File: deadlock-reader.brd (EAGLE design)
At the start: 49.2 x 49.5 mm, 49 parts, among them IC1 LM386M-1, IC2 STM32F072XX, IC3 MCP16301/H, IC4 MAX3232CSE, J1 RJ12 6p6c, X1 MINI-USB-SCHIELD-32005-301

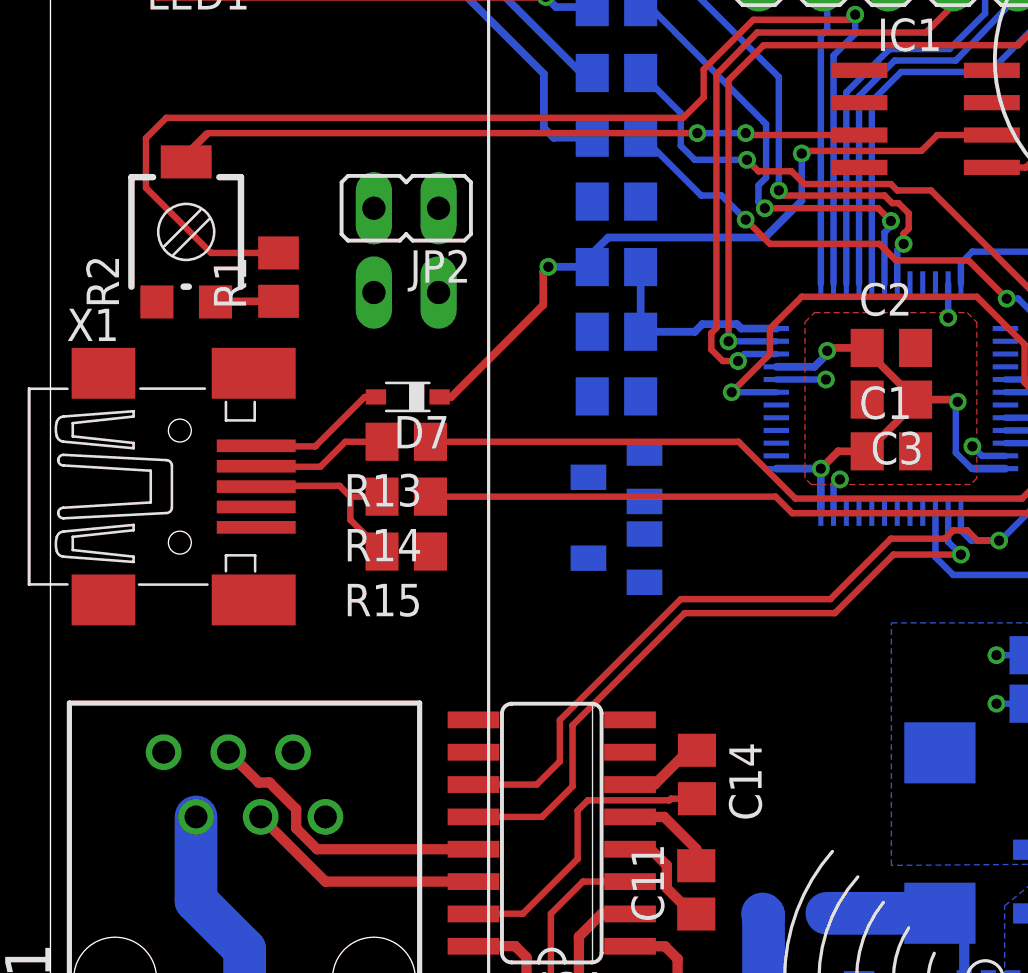
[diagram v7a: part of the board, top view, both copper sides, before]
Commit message: [WIP] Route misc remaining signal lines
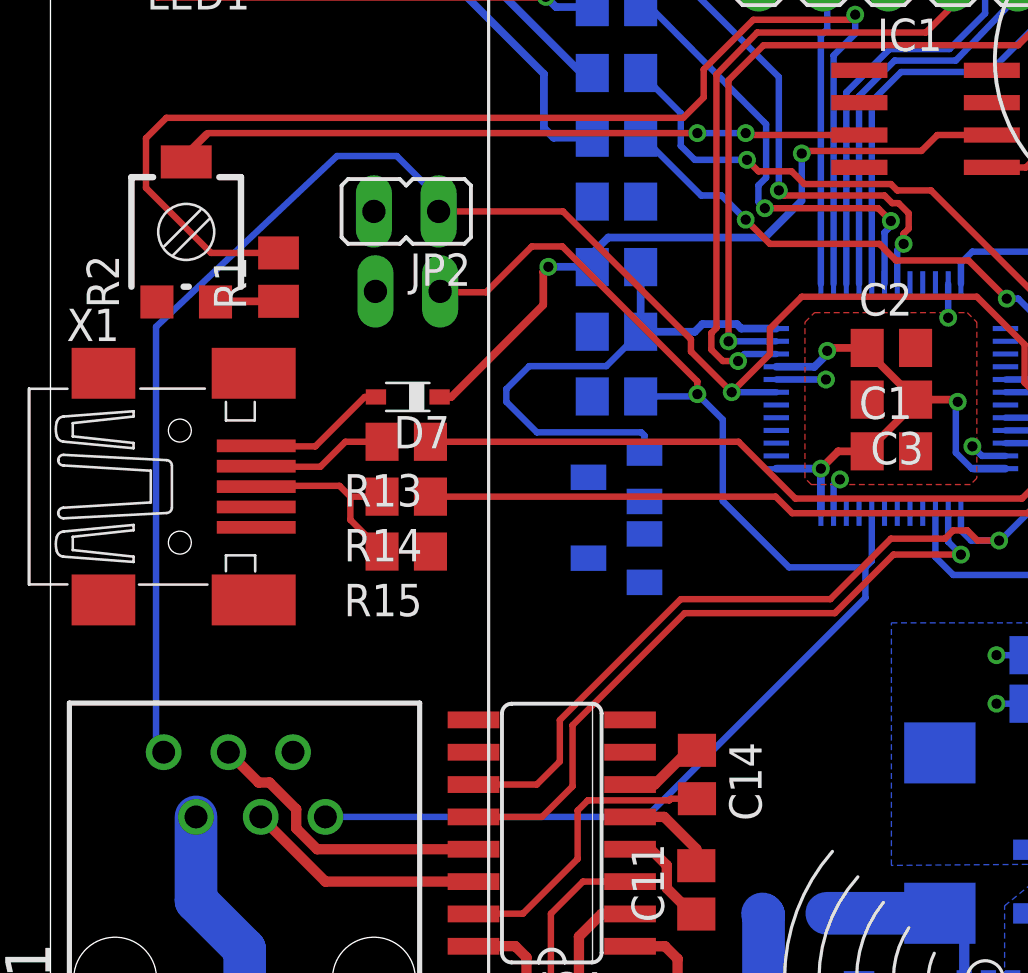
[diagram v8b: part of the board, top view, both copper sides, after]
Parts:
- moved JP2 0.12 mm to (14.0, 36.5)
- moved JP1 0.07 mm to (14.0, 33.3), turned to 270 degrees
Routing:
- net BOOT0: track 0.00 -> 55.3 mm, vias 0 -> 1
- net RST: track 29.1 -> 75.7 mm
- net V_SENSE: track 8.06 -> 21.4 mm
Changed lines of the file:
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@@
 <setting verticaltext="up"/>
 </settings>
-<grid distance="0.05" unitdist="mm" unit="mm" style="dots" multiple="5" display="yes" altdistance="0.125" altunitdist="mm" altunit="mm"/>
+<grid distance="0.1" unitdist="mm" unit="mm" style="dots" multiple="5" display="yes" altdistance="0.125" altunitdist="mm" altunit="mm"/>
 <layers>
 <layer number="1" name="Top" color="4" fill="1" visible="yes" active="yes"/>
@@
 <attribute name="MF" value="" x="7.62" y="6.35" size="1.778" layer="27" display="off"/>
 </element>
-<element name="JP1" library="jumper" package="JP1" value="BOOT" x="13.97" y="33.29" rot="MR90"/>
-<element name="JP2" library="jumper" package="JP1" value="RESET" x="13.97" y="36.6" rot="R90"/>
+<element name="JP1" library="jumper" package="JP1" value="BOOT" x="14.03" y="33.335" rot="MR270"/>
+<element name="JP2" library="jumper" package="JP1" value="RESET" x="13.97" y="36.475" rot="R90"/>
 <element name="JP3" library="pinhead" package="1X06" value="" x="45.74" y="28.545" rot="MR270"/>
 <element name="L1" library="rcl" package="PIS2816" value="15uH" x="42.545" y="12.065" rot="MR180"/>
@@
 <wire x1="2.08" y1="30.12" x2="4.18" y2="32.92" width="0" layer="19" extent="1-1"/>
 <wire x1="2.08" y1="21.22" x2="7.98" y2="21.22" width="0" layer="19" extent="1-1"/>
-<wire x1="12.7" y1="36.6" x2="7.98" y2="30.12" width="0" layer="19" extent="1-1"/>
-<wire x1="9.93" y1="46.75" x2="12.7" y2="36.6" width="0" layer="19" extent="1-1"/>
+<wire x1="12.7" y1="36.475" x2="7.98" y2="30.12" width="0" layer="19" extent="1-1"/>
+<wire x1="9.93" y1="46.75" x2="12.7" y2="36.475" width="0" layer="19" extent="1-1"/>
 </signal>
 <signal name="N$1">
@@
 <contactref element="JP1" pad="1"/>
 <contactref element="R6" pad="2"/>
-<wire x1="23.175" y1="29.21" x2="32.25" y2="24.625" width="0" layer="19" extent="16-16"/>
-<wire x1="12.7" y1="33.29" x2="23.175" y2="29.21" width="0" layer="19" extent="16-16"/>
-<wire x1="10.795" y1="12.7" x2="23.175" y2="29.21" width="0" layer="19" extent="16-16"/>
+<wire x1="32.25" y1="24.625" x2="32.25" y2="22.75" width="0.254" layer="16"/>
+<wire x1="32.25" y1="22.75" x2="32" y2="22.5" width="0.254" layer="16"/>
+<wire x1="32" y1="22.5" x2="29" y2="22.5" width="0.254" layer="16"/>
+<wire x1="29" y1="22.5" x2="26.4" y2="25.1" width="0.254" layer="16"/>
+<wire x1="26.4" y1="25.1" x2="26.4" y2="28.3" width="0.254" layer="16"/>
+<wire x1="26.4" y1="28.3" x2="25.4" y2="29.3" width="0.254" layer="16"/>
+<via x="25.4" y="29.3" extent="1-16" drill="0.4"/>
+<wire x1="25.4" y1="29.3" x2="25.4" y2="29.8" width="0.254" layer="1"/>
+<wire x1="25.4" y1="29.8" x2="20.1" y2="35.1" width="0.254" layer="1"/>
+<wire x1="20.1" y1="35.1" x2="18.9" y2="35.1" width="0.254" layer="1"/>
+<wire x1="18.9" y1="35.1" x2="17.1" y2="33.3" width="0.254" layer="1"/>
+<wire x1="17.1" y1="33.3" x2="15.335" y2="33.3" width="0.254" layer="1"/>
+<wire x1="15.335" y1="33.3" x2="15.3" y2="33.335" width="0.254" layer="1"/>
+<wire x1="10.795" y1="12.7" x2="23.4" y2="12.7" width="0.254" layer="16"/>
+<wire x1="23.4" y1="12.7" x2="32" y2="21.3" width="0.254" layer="16"/>
+<wire x1="32" y1="21.3" x2="32" y2="22.5" width="0.254" layer="16"/>
+<wire x1="23.175" y1="29.21" x2="25.31" y2="29.21" width="0.254" layer="16"/>
+<wire x1="25.31" y1="29.21" x2="25.4" y2="29.3" width="0.254" layer="16"/>
 </signal>
 <signal name="RST">
@@
 <via x="26.75" y="29.375" extent="1-16" drill="0.4"/>
 <wire x1="26.75" y1="29.375" x2="28.5" y2="29.375" width="0.254" layer="16"/>
-<wire x1="15.24" y1="36.6" x2="26.75" y2="29.375" width="0" layer="19" extent="1-1"/>
-<wire x1="4.445" y1="15.24" x2="15.24" y2="36.6" width="0" layer="19" extent="1-1"/>
+<wire x1="15.24" y1="36.475" x2="20.125" y2="36.475" width="0.254" layer="1"/>
+<wire x1="20.125" y1="36.475" x2="25.15" y2="31.45" width="0.254" layer="1"/>
+<wire x1="25.15" y1="31.45" x2="25.15" y2="30.975" width="0.254" layer="1"/>
+<wire x1="25.15" y1="30.975" x2="26.75" y2="29.375" width="0.254" layer="1"/>
+<wire x1="4.145" y1="31.945" x2="11.25" y2="38.65" width="0.254" layer="16"/>
+<wire x1="11.25" y1="38.65" x2="13.6" y2="38.65" width="0.254" layer="16"/>
+<wire x1="13.6" y1="38.65" x2="15.1" y2="37.15" width="0.254" layer="16"/>
+<wire x1="15.1" y1="37.15" x2="15.1" y2="36.615" width="0.254" layer="16"/>
+<wire x1="15.1" y1="36.615" x2="15.24" y2="36.475" width="0.254" layer="16"/>
+<wire x1="4.145" y1="31.945" x2="4.145" y2="15.54" width="0.254" layer="16"/>
+<wire x1="4.145" y1="15.54" x2="4.445" y2="15.24" width="0.254" layer="16"/>
 </signal>
 <signal name="RDR_TXD/SWDIO">
@@
 <wire x1="16.6166" y1="7.625" x2="16.6116" y2="7.62" width="0.4064" layer="1"/>
 <wire x1="21.275" y1="36.86" x2="27.815" y2="45.845" width="0" layer="19" extent="16-16"/>
-<wire x1="15.24" y1="33.29" x2="21.275" y2="36.86" width="0" layer="19" extent="16-16"/>
-<wire x1="21.125" y1="26.035" x2="15.24" y2="33.29" width="0" layer="19" extent="16-16"/>
-<wire x1="23.325" y1="23.81" x2="21.125" y2="26.035" width="0" layer="19" extent="16-16"/>
-<wire x1="28.5" y1="26.375" x2="23.325" y2="23.81" width="0" layer="19" extent="16-16"/>
+<wire x1="12.76" y1="33.335" x2="21.275" y2="36.86" width="0" layer="19" extent="16-16"/>
+<wire x1="28.5" y1="30.375" x2="21.275" y2="36.86" width="0" layer="19" extent="16-16"/>
 <wire x1="35.75" y1="33.625" x2="32.07" y2="31.115" width="0" layer="19" extent="1-16"/>
+<wire x1="23.325" y1="23.81" x2="28.5" y2="26.375" width="0" layer="19" extent="16-16"/>
+<wire x1="21.125" y1="26.035" x2="23.325" y2="23.81" width="0" layer="19" extent="16-16"/>
 <wire x1="14.92" y1="23.12" x2="21.125" y2="26.035" width="0" layer="19" extent="1-16"/>
 <wire x1="41.38" y1="19.05" x2="37.5" y2="26.375" width="0" layer="19" extent="16-16"/>
@@
 <wire x1="25.3" y1="31.75" x2="23.175" y2="31.75" width="0.3048" layer="16"/>
 <wire x1="26.95" y1="32.05" x2="25.6" y2="32.05" width="0.3048" layer="16"/>
-<wire x1="23.325" y1="26.985" x2="23.175" y2="31.75" width="0" layer="19" extent="16-16"/>
+<wire x1="23.325" y1="26.985" x2="23.325" y2="27.675" width="0.254" layer="16"/>
+<wire x1="23.325" y1="27.675" x2="23.2" y2="27.8" width="0.254" layer="16"/>
+<wire x1="23.2" y1="27.8" x2="19.1" y2="27.8" width="0.254" layer="16"/>
+<wire x1="19.1" y1="27.8" x2="17.9" y2="29" width="0.254" layer="16"/>
+<wire x1="17.9" y1="29" x2="17.9" y2="29.5" width="0.254" layer="16"/>
+<wire x1="17.9" y1="29.5" x2="18.8" y2="30.4" width="0.254" layer="16"/>
+<wire x1="18.8" y1="30.4" x2="21.825" y2="30.4" width="0.254" layer="16"/>
+<wire x1="21.825" y1="30.4" x2="23.175" y2="31.75" width="0.254" layer="16"/>
 </signal>
 <signal name="N$14">
